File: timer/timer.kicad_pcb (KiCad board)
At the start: 2 copper layers, 23 parts, among them J1 Conn_01x02_Female, Q1 BC546, Q2 BC546, U1 LM339, U2 7402

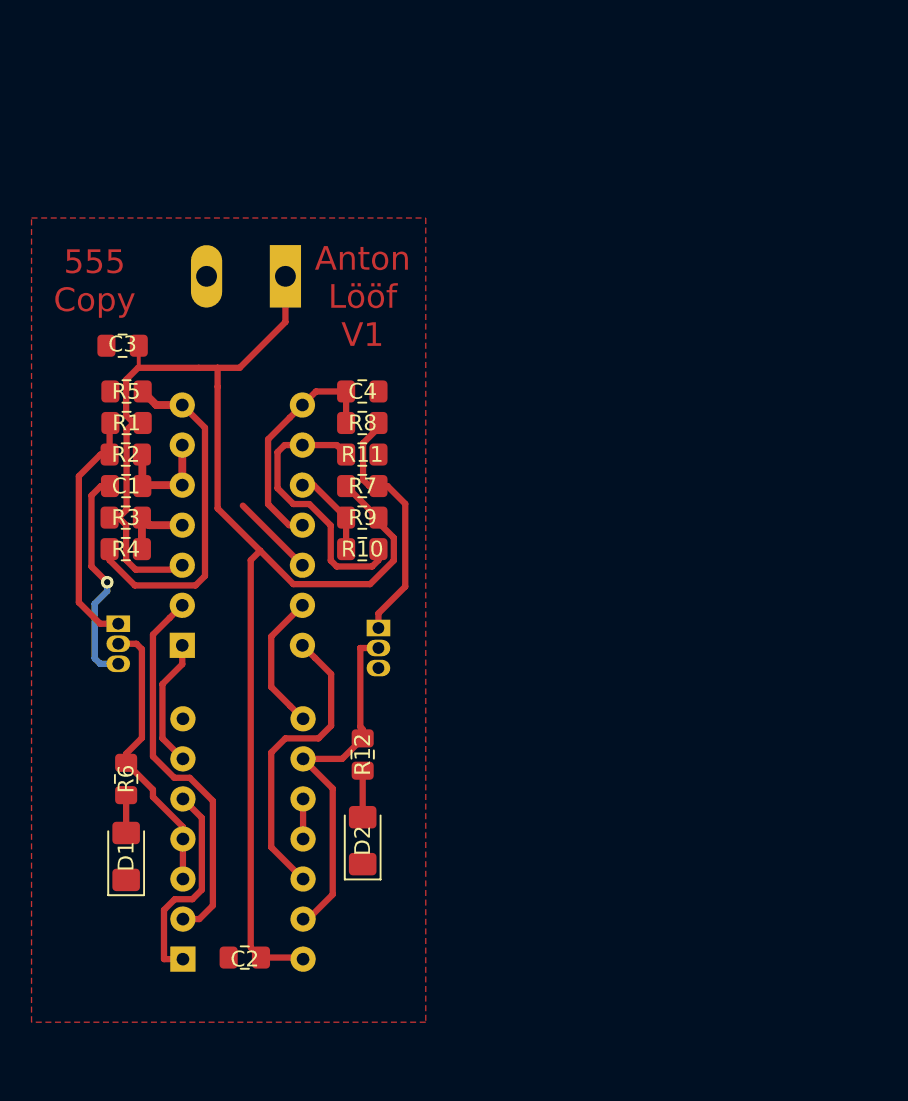
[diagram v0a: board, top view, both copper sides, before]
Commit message: Start using opamp that can ouput stuff
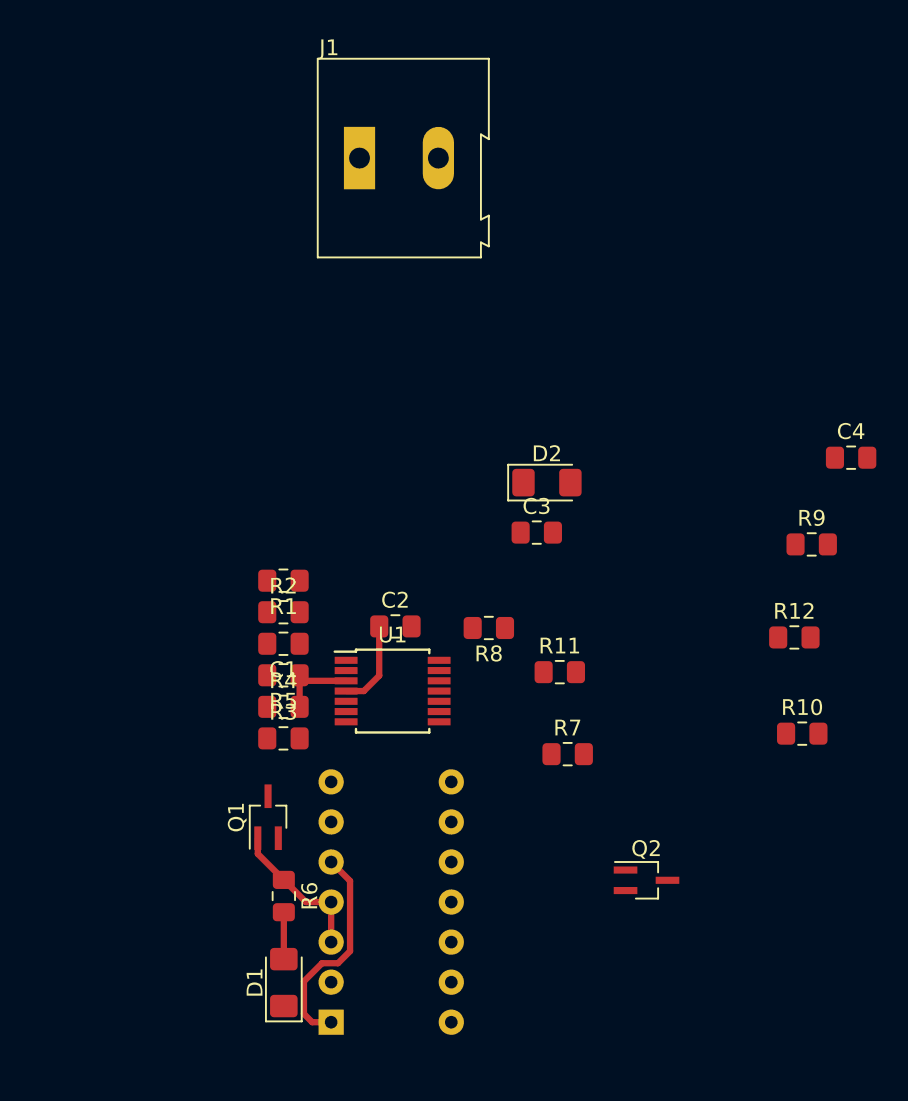
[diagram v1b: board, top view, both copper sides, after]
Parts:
- J1: moved to F.Cu
- Q1, Q2: value BC546 -> BC847; footprint Package_TO_SOT_THT:TO-92_Inline -> Package_TO_SOT_SMD:SOT-323_SC-70_Handsoldering; moved to F.Cu
- U1: value LM339 -> LM2902; footprint Package_DIP:DIP-14_W7.62mm -> Package_SO:TSSOP-14_4.4x5mm_P0.65mm; moved to F.Cu
- moved C4 31.3 mm to (161.0, 86.2)
- moved R10 30.3 mm to (157.9, 103.7)
- moved C3 28.8 mm to (141.0, 91.0), turned to 0 degrees
- moved R9 28.6 mm to (158.5, 91.7), turned to 0 degrees
- moved R12 28.4 mm to (157.4, 97.6), turned to 0 degrees
- moved D2 25.5 mm to (141.7, 87.8), turned to 0 degrees
- moved Q2 23.3 mm to (148.0, 113.0), turned to 0 degrees
- moved C2 23.1 mm to (132.1, 96.9), turned to 0 degrees
- moved R7 21.4 mm to (143.0, 105.0)
- moved R5 20.6 mm to (125.0, 100.0)
- moved R11 18.6 mm to (142.5, 99.8)
- moved R3 17.2 mm to (125.0, 104.0)
- moved Q1 15.5 mm to (124.0, 109.0), turned to 90 degrees
- moved R8 15.3 mm to (138.0, 97.0)
- moved R2 14.1 mm to (125.0, 96.0)
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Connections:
- Q1 pad 2: Net-(Q1-Pad2) -> GND
- Q1 pad 3: GND -> Net-(Q1-Pad3)
- Q2 pad 2: Net-(Q2-Pad2) -> GND
- Q2 pad 3: GND -> Net-(Q2-Pad3)
- R1 pad 2: Net-(Q1-Pad1) -> Net-(Q1-Pad3)
- R12 pad 1: Net-(Q2-Pad2) -> Net-(Q2-Pad1)
- R2 pad 1: Net-(Q1-Pad1) -> Net-(Q1-Pad3)
- R6 pad 1: Net-(Q1-Pad2) -> Net-(Q1-Pad1)
- R7 pad 2: Net-(Q2-Pad1) -> Net-(Q2-Pad3)
- R8 pad 1: Net-(Q2-Pad1) -> Net-(Q2-Pad3)
- U1 pad 10: Net-(R10-Pad1) -> Net-(C4-Pad1)
- U1 pad 11: Net-(C4-Pad1) -> GND
- U1 pad 12: GND -> Net-(R10-Pad2)
- U1 pad 13: Net-(U1-Pad13) -> Net-(C4-Pad1)
- U1 pad 2: Net-(U1-Pad2) -> Net-(C1-Pad1)
- U1 pad 3: +5V -> Net-(R4-Pad2)
- U1 pad 4: Net-(R3-Pad2) -> +5V
- U1 pad 6: Net-(C1-Pad1) -> Net-(R3-Pad2)
- U1 pad 7: Net-(R4-Pad2) -> Net-(U1-Pad7)
- U1 pad 8: Net-(C4-Pad1) -> Net-(U1-Pad8)
- U1 pad 9: Net-(R10-Pad2) -> Net-(R10-Pad1)
- U2 pad 13: Net-(Q2-Pad2) -> Net-(Q2-Pad1)
- U2 pad 2: Net-(U1-Pad2) -> Net-(U1-Pad7)
- U2 pad 3: Net-(Q1-Pad2) -> Net-(Q1-Pad1)
- U2 pad 4: Net-(Q1-Pad2) -> Net-(Q1-Pad1)
- U2 pad 8: Net-(U1-Pad13) -> Net-(U1-Pad8)
- U2 pad 9: Net-(Q2-Pad2) -> Net-(Q2-Pad1)
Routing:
- net +5V: track 91.0 -> 5.63 mm
- net Net-(U1-Pad2): track 24.3 -> 0.00 mm
- net Net-(Q2-Pad2): track 23.2 -> 0.00 mm
- net GND: track 19.5 -> 0.00 mm, vias 1 -> 0
- net Net-(U1-Pad14): track 19.2 -> 0.00 mm
- net Net-(Q1-Pad2): track 18.1 -> 0.00 mm
- net Net-(R10-Pad2): track 17.9 -> 0.00 mm
- net Net-(R4-Pad2): track 22.0 -> 5.09 mm
- net Net-(Q2-Pad1): track 16.3 -> 0.00 mm
- net Net-(C4-Pad1): track 15.1 -> 0.00 mm
- net Net-(U1-Pad13): track 8.86 -> 0.00 mm
- net Net-(U1-Pad1): track 8.26 -> 0.00 mm
- net Net-(C1-Pad1): track 7.11 -> 0.00 mm
- net Net-(Q1-Pad1): track 15.6 -> 9.45 mm
- net Net-(R10-Pad1): track 5.62 -> 0.00 mm
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- removed copper zone on F.Cu, net GND
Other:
- board text removed: "555 Copy"
- board text removed: "Anton Lööf V1"

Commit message: Finalize rev2 pcb
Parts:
- D1, D2, J1: moved to B.Cu
- moved D2 33.3 mm to (139.0, 121.0), turned to 90 degrees
- moved C3 32.3 mm to (132.0, 122.0), turned to 180 degrees
- moved J1 26.2 mm to (134.6, 93.0), turned to 180 degrees
- moved C4 24.9 mm to (139.0, 98.0)
- moved R12 24.6 mm to (139.0, 114.0), turned to 270 degrees
- moved R9 23.0 mm to (139.0, 104.0), turned to 180 degrees
- moved R10 18.9 mm to (139.0, 102.0)
- moved R7 11.7 mm to (139.0, 94.0)
- moved Q2 9.85 mm to (139.0, 109.0), turned to 90 degrees
- moved R1 6.00 mm to (125.0, 100.0)
- moved R4 6.00 mm to (125.0, 96.0)
- moved C1 4.00 mm to (125.0, 102.0)
- moved R11 3.53 mm to (139.0, 100.0)
- moved R5 2.00 mm to (125.0, 98.0)
- moved R2 2.00 mm to (125.0, 94.0)
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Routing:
- net +5V: track 5.63 -> 60.2 mm
- net GND: track 0.00 -> 37.8 mm, vias 0 -> 7
- net Net-(R3-Pad2): track 0.00 -> 28.4 mm
- net Net-(U1-Pad14): track 0.00 -> 24.1 mm, vias 0 -> 2
- net Net-(C4-Pad1): track 0.00 -> 19.4 mm
- net Net-(C1-Pad1): track 0.00 -> 18.6 mm, vias 0 -> 2
- net Net-(U1-Pad7): track 0.00 -> 18.5 mm
- net Net-(Q2-Pad3): track 0.00 -> 16.5 mm
- net Net-(Q1-Pad3): track 0.00 -> 16.0 mm
- net Net-(U1-Pad1): track 0.00 -> 14.0 mm, vias 0 -> 2
- net Net-(Q2-Pad1): track 0.00 -> 14.0 mm
- net Net-(R10-Pad2): track 0.00 -> 6.17 mm
- net Net-(R10-Pad1): track 0.00 -> 5.27 mm
- net Net-(D2-Pad2): track 0.00 -> 4.46 mm, vias 0 -> 1
- net Net-(U1-Pad8): track 0.00 -> 4.19 mm
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- added copper zone on B.Cu, net GND
- added copper zone on F.Cu, net GND
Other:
- board outline added: 24 x 34 mm
- board text added: "555 Copy"
- board text added: "Anton Lööf V2"
